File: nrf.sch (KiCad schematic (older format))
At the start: 6 parts, among them SW1 SW_DPST_x2, U1 BLYST-NRF52832-NANO, U2 Oled_128x64_SSD1306

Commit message: More power setup
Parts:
- added SW2: MID, my-fp-library:Tact_SW_3x6x3.5, symbol Switch:SW_DPST_x2
- added SW3: DWN, my-fp-library:Tact_SW_3x6x3.5, symbol Switch:SW_DPST_x2
- SW1: value SW_DPST_x2 -> UP; footprint Buttons_Switches_SMD:SW_DIP_x2_W5.08mm_Slide_Copal_CHS-A -> my-fp-library:Tact_SW_3x6x3.5
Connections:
- net labels added: BTN_2, BTN_3, I2C_SCL, I2C_SDA, SCL, SDA
- wire segments 55 -> 66
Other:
- moved on the sheet: SW1A
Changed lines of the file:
@@
 L Switch:SW_DPST_x2 SW1
 U 1 1 5D072A19
-P 1200 2450
-F 0 "SW1" H 1200 2685 50  0000 C CNN
-F 1 "SW_DPST_x2" H 1200 2594 50  0000 C CNN
-F 2 "Buttons_Switches_SMD:SW_DIP_x2_W5.08mm_Slide_Copal_CHS-A" H 1200 2450 50  0001 C CNN
-F 3 "" H 1200 2450 50  0001 C CNN
-	1    1200 2450
+P 5150 1150
+F 0 "SW1" H 5150 1385 50  0000 C CNN
+F 1 "UP" H 5150 1294 50  0000 C CNN
+F 2 "my-fp-library:Tact_SW_3x6x3.5" H 5150 1150 50  0001 C CNN
+F 3 "" H 5150 1150 50  0001 C CNN
+	1    5150 1150
 	1    0    0    -1
 $EndComp
@@
 L power:GND #PWR0101
 U 1 1 5D072B76
-P 850 2650
-F 0 "#PWR0101" H 850 2400 50  0001 C CNN
-F 1 "GND" H 855 2477 50  0000 C CNN
-F 2 "" H 850 2650 50  0001 C CNN
-F 3 "" H 850 2650 50  0001 C CNN
-	1    850  2650
+P 4550 2200
+F 0 "#PWR0101" H 4550 1950 50  0001 C CNN
+F 1 "GND" H 4555 2027 50  0000 C CNN
+F 2 "" H 4550 2200 50  0001 C CNN
+F 3 "" H 4550 2200 50  0001 C CNN
+	1    4550 2200
 	1    0    0    -1
 $EndComp
-Wire Wire Line
-	1000 2450 850  2450
-Wire Wire Line
-	850  2450 850  2650
 Text GLabel 3550 1350 2    50   Output ~ 0
 MOTOR_PWM
@@
 F1 "accelerometer.sch" 50
 $EndSheet
+$Comp
+L Switch:SW_DPST_x2 SW3
+U 1 1 5D0B8B59
+P 5150 1950
+F 0 "SW3" H 5150 2185 50  0000 C CNN
+F 1 "DWN" H 5150 2094 50  0000 C CNN
+F 2 "my-fp-library:Tact_SW_3x6x3.5" H 5150 1950 50  0001 C CNN
+F 3 "" H 5150 1950 50  0001 C CNN
+	1    5150 1950
+	1    0    0    -1
+$EndComp
+Wire Wire Line
+	5350 1950 5850 1950
+Wire Wire Line
+	5350 1550 5850 1550
+Wire Wire Line
+	5350 1150 5850 1150
+Wire Wire Line
+	4950 1950 4550 1950
+Wire Wire Line
+	4550 1950 4550 2200
+Wire Wire Line
+	4950 1550 4550 1550
+Wire Wire Line
+	4550 1550 4550 1950
+Connection ~ 4550 1950
+Wire Wire Line
+	4950 1150 4550 1150
+Wire Wire Line
+	4550 1150 4550 1550
+Connection ~ 4550 1550
+Text Label 5600 1150 0    50   ~ 0
+BTN_1
+Text Label 5600 1550 0    50   ~ 0
+BTN_2
+Text Label 5600 1950 0    50   ~ 0
+BTN_3
+Wire Wire Line
+	1800 2550 1400 2550
+Wire Wire Line
+	1800 2350 1400 2350
+Text Label 1450 2550 0    50   ~ 0
+BTN_2
+Text Label 1450 2350 0    50   ~ 0
+BTN_3
+Wire Wire Line
+	1800 1350 1400 1350
+Wire Wire Line
+	1800 1450 1400 1450
+Text Label 1450 1350 0    50   ~ 0
+SDA
+Text Label 1450 1450 0    50   ~ 0
+SCL
+Text GLabel 1400 1450 0    50   Output ~ 0
+I2C_SCL
+Text GLabel 1400 1350 0    50   Output ~ 0
+I2C_SDA
+$Comp
+L Switch:SW_DPST_x2 SW2
+U 1 1 5D0D8973
+P 5150 1550
+F 0 "SW2" H 5150 1785 50  0000 C CNN
+F 1 "MID" H 5150 1694 50  0000 C CNN
+F 2 "my-fp-library:Tact_SW_3x6x3.5" H 5150 1550 50  0001 C CNN
+F 3 "" H 5150 1550 50  0001 C CNN
+	1    5150 1550
+	1    0    0    -1
+$EndComp
 $EndSCHEMATC

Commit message: Connectors
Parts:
- added J2: Conn_01x05, Pin_Headers:Pin_Header_Straight_1x05_Pitch1.27mm, symbol Connector_Generic:Conn_01x05
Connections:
- net labels added: RESET, SWDCLK, SWDIO
- net labels removed: GND, VDD
- wire segments 66 -> 79
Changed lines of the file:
@@
-	1    0    0    -1
-$EndComp
-$Comp
-L power:GND #PWR0102
-U 1 1 5CE49E1D
-P 7500 2050
-F 0 "#PWR0102" H 7500 1800 50  0001 C CNN
-F 1 "GND" H 7505 1877 50  0000 C CNN
-F 2 "" H 7500 2050 50  0001 C CNN
-F 3 "" H 7500 2050 50  0001 C CNN
-	1    7500 2050
 	1    0    0    -1
 $EndComp
@@
 Wire Wire Line
 	7300 2550 7300 2500
-$Comp
-L power:GND #PWR0103
-U 1 1 5CE4A4F8
-P 7450 2650
-F 0 "#PWR0103" H 7450 2400 50  0001 C CNN
-F 1 "GND" H 7455 2477 50  0000 C CNN
-F 2 "" H 7450 2650 50  0001 C CNN
-F 3 "" H 7450 2650 50  0001 C CNN
-	1    7450 2650
-	1    0    0    -1
-$EndComp
 Wire Wire Line
 	8100 2750 7750 2750
@@
 Wire Wire Line
 	7750 2650 7450 2650
-$Comp
-L power:VDD #PWR0105
-U 1 1 5CE4AA70
-P 7300 2500
-F 0 "#PWR0105" H 7300 2350 50  0001 C CNN
-F 1 "VDD" H 7317 2673 50  0000 C CNN
-F 2 "" H 7300 2500 50  0001 C CNN
-F 3 "" H 7300 2500 50  0001 C CNN
-	1    7300 2500
-	1    0    0    -1
-$EndComp
-$Comp
-L power:GND #PWR0106
-U 1 1 5CE4AB71
-P 7400 3150
-F 0 "#PWR0106" H 7400 2900 50  0001 C CNN
-F 1 "GND" H 7405 2977 50  0000 C CNN
-F 2 "" H 7400 3150 50  0001 C CNN
-F 3 "" H 7400 3150 50  0001 C CNN
-	1    7400 3150
-	1    0    0    -1
-$EndComp
 Wire Wire Line
 	8100 3150 8050 3150
@@
 Text Label 7750 3850 0    50   ~ 0
 MOSI
-$Comp
-L power:GND #PWR01
-U 1 1 5CE4E69E
-P 7450 4200
-F 0 "#PWR01" H 7450 3950 50  0001 C CNN
-F 1 "GND" H 7455 4027 50  0000 C CNN
-F 2 "" H 7450 4200 50  0001 C CNN
-F 3 "" H 7450 4200 50  0001 C CNN
-	1    7450 4200
-	1    0    0    -1
-$EndComp
 Wire Wire Line
 	8000 4050 7450 4050
@@
 Wire Wire Line
 	7450 4550 7450 4600
-$Comp
-L power:GND #PWR02
-U 1 1 5CE53560
-P 7450 5000
-F 0 "#PWR02" H 7450 4750 50  0001 C CNN
-F 1 "GND" H 7455 4827 50  0000 C CNN
-F 2 "" H 7450 5000 50  0001 C CNN
-F 3 "" H 7450 5000 50  0001 C CNN
-	1    7450 5000
-	1    0    0    -1
-$EndComp
 Wire Wire Line
 	7450 4900 7450 5000
-$Comp
-L power:GND #PWR03
-U 1 1 5CE53F0B
-P 7900 5050
-F 0 "#PWR03" H 7900 4800 50  0001 C CNN
-F 1 "GND" H 7905 4877 50  0000 C CNN
-F 2 "" H 7900 5050 50  0001 C CNN
-F 3 "" H 7900 5050 50  0001 C CNN
-	1    7900 5050
-	1    0    0    -1
-$EndComp
 Wire Wire Line
 	8100 4850 7900 4850
@@
 Wire Wire Line
 	7900 4950 7900 5050
-$Comp
-L power:VDD #PWR0104
-U 1 1 5CE5A0A2
-P 7200 2850
-F 0 "#PWR0104" H 7200 2700 50  0001 C CNN
-F 1 "VDD" H 7217 3023 50  0000 C CNN
-F 2 "" H 7200 2850 50  0001 C CNN
-F 3 "" H 7200 2850 50  0001 C CNN
-	1    7200 2850
-	1    0    0    -1
-$EndComp
 Wire Wire Line
 	8100 2850 7200 2850
@@
 	1    0    0    -1
 $EndComp
-$Comp
-L power:GND #PWR0101
-U 1 1 5D072B76
-P 4550 2200
-F 0 "#PWR0101" H 4550 1950 50  0001 C CNN
-F 1 "GND" H 4555 2027 50  0000 C CNN
-F 2 "" H 4550 2200 50  0001 C CNN
-F 3 "" H 4550 2200 50  0001 C CNN
-	1    4550 2200
-	1    0    0    -1
-$EndComp
 Text GLabel 3550 1350 2    50   Output ~ 0
 MOTOR_PWM
@@
 	4950 1950 4550 1950
 Wire Wire Line
-	4550 1950 4550 2200
-Wire Wire Line
 	4950 1550 4550 1550
 Wire Wire Line
 	4550 1550 4550 1950
-Connection ~ 4550 1950
 Wire Wire Line
 	4950 1150 4550 1150
@@
 Text Label 1450 1350 0    50   ~ 0
 SDA
-Text Label 1450 1450 0    50   ~ 0
-SCL
-Text GLabel 1400 1450 0    50   Output ~ 0
+Text GLabel 1400 1550 0    50   Output ~ 0
 I2C_SCL
 Text GLabel 1400 1350 0    50   Output ~ 0
@@
 	1    0    0    -1
 $EndComp
+$Comp
+L Connector_Generic:Conn_01x05 J2
+U 1 1 5D0EA690
+P 5000 3300
+F 0 "J2" H 5080 3342 50  0000 L CNN
+F 1 "Conn_01x05" H 5080 3251 50  0000 L CNN
+F 2 "Pin_Headers:Pin_Header_Straight_1x05_Pitch1.27mm" H 5000 3300 50  0001 C CNN
+F 3 "~" H 5000 3300 50  0001 C CNN
+	1    5000 3300
+	1    0    0    -1
+$EndComp
+Connection ~ 4550 1950
+Wire Wire Line
+	4550 1950 4550 2200
+$Comp
+L power:(GND) #PWR01
+U 1 1 5D0FADC1
+P 4550 2200
+F 0 "#PWR01" H 4550 2200 30  0001 C CNN
+F 1 "(GND)" H 4550 2200 30  0001 C CNN
+F 2 "" H 4550 2200 60  0000 C CNN
+F 3 "" H 4550 2200 60  0000 C CNN
+	1    4550 2200
+	1    0    0    -1
+$EndComp
+$Comp
+L power:(GND) #PWR011
+U 1 1 5D0FAF36
+P 7450 2700
+F 0 "#PWR011" H 7450 2700 30  0001 C CNN
+F 1 "(GND)" H 7450 2700 30  0001 C CNN
+F 2 "" H 7450 2700 60  0000 C CNN
+F 3 "" H 7450 2700 60  0000 C CNN
+	1    7450 2700
+	1    0    0    -1
+$EndComp
+$Comp
+L power:(GND) #PWR010
+U 1 1 5D0FAF53
+P 7400 3200
+F 0 "#PWR010" H 7400 3200 30  0001 C CNN
+F 1 "(GND)" H 7400 3200 30  0001 C CNN
+F 2 "" H 7400 3200 60  0000 C CNN
+F 3 "" H 7400 3200 60  0000 C CNN
+	1    7400 3200
+	1    0    0    -1
+$EndComp
+$Comp
+L power:(GND) #PWR014
+U 1 1 5D0FAF7A
+P 7500 2100
+F 0 "#PWR014" H 7500 2100 30  0001 C CNN
+F 1 "(GND)" H 7500 2100 30  0001 C CNN
+F 2 "" H 7500 2100 60  0000 C CNN
+F 3 "" H 7500 2100 60  0000 C CNN
+	1    7500 2100
+	1    0    0    -1
+$EndComp
+Wire Wire Line
+	7500 2050 7500 2100
+Wire Wire Line
+	7450 2650 7450 2700
+Wire Wire Line
+	7400 3150 7400 3200
+$Comp
+L power:(GND) #PWR012
+U 1 1 5D0FFE5A
+P 7450 4200
+F 0 "#PWR012" H 7450 4200 30  0001 C CNN
+F 1 "(GND)" H 7450 4200 30  0001 C CNN
+F 2 "" H 7450 4200 60  0000 C CNN
+F 3 "" H 7450 4200 60  0000 C CNN
+	1    7450 4200
+	1    0    0    -1
+$EndComp
+$Comp
+L power:(GND) #PWR013
+U 1 1 5D0FFE77
+P 7450 5000
+F 0 "#PWR013" H 7450 5000 30  0001 C CNN
+F 1 "(GND)" H 7450 5000 30  0001 C CNN
+F 2 "" H 7450 5000 60  0000 C CNN
+F 3 "" H 7450 5000 60  0000 C CNN
+	1    7450 5000
+	1    0    0    -1
+$EndComp
+$Comp
+L power:(GND) #PWR015
+U 1 1 5D0FFEAF
+P 7900 5050
+F 0 "#PWR015" H 7900 5050 30  0001 C CNN
+F 1 "(GND)" H 7900 5050 30  0001 C CNN
+F 2 "" H 7900 5050 60  0000 C CNN
+F 3 "" H 7900 5050 60  0000 C CNN
+	1    7900 5050
+	1    0    0    -1
+$EndComp
+$Comp
+L power:+3.3 #PWR09
+U 1 1 5D100235
+P 7300 2500
+F 0 "#PWR09" H 7300 2550 30  0001 C CNN
+F 1 "+3.3" H 7300 2633 50  0000 C CNN
+F 2 "" H 7300 2500 60  0000 C CNN
+F 3 "" H 7300 2500 60  0000 C CNN
+	1    7300 2500
+	1    0    0    -1
+$EndComp
+$Comp
+L power:+3.3 #PWR08
+U 1 1 5D1002BF
+P 7200 2850
+F 0 "#PWR08" H 7200 2900 30  0001 C CNN
+F 1 "+3.3" H 7200 2983 50  0000 C CNN
+F 2 "" H 7200 2850 60  0000 C CNN
+F 3 "" H 7200 2850 60  0000 C CNN
+	1    7200 2850
+	1    0    0    -1
+$EndComp
+$Comp
+L power:(GND) #PWR03
+U 1 1 5D1005C9
+P 4700 3750
+F 0 "#PWR03" H 4700 3750 30  0001 C CNN
+F 1 "(GND)" H 4700 3750 30  0001 C CNN
+F 2 "" H 4700 3750 60  0000 C CNN
+F 3 "" H 4700 3750 60  0000 C CNN
+	1    4700 3750
+	1    0    0    -1
+$EndComp
+$Comp
+L power:+3.3 #PWR02
+U 1 1 5D1005E6
+P 4700 2950
+F 0 "#PWR02" H 4700 3000 30  0001 C CNN
+F 1 "+3.3" H 4700 3083 50  0000 C CNN
+F 2 "" H 4700 2950 60  0000 C CNN
+F 3 "" H 4700 2950 60  0000 C CNN
+	1    4700 2950
+	1    0    0    -1
+$EndComp
+Wire Wire Line
+	4800 3100 4700 3100
+Wire Wire Line
+	4700 3100 4700 2950
+Wire Wire Line
+	4800 3500 4700 3500
+Wire Wire Line
+	4700 3500 4700 3750
+Wire Wire Line
+	4800 3400 4400 3400
+Wire Wire Line
+	1800 1550 1400 1550
+Text Label 1450 1550 0    50   ~ 0
+SCL
+Text Label 1450 1450 0    50   ~ 0
+RESET
+Text Label 4450 3400 0    50   ~ 0
+RESET
+Wire Wire Line
+	4800 3300 4400 3300
+Wire Wire Line
+	4800 3200 4400 3200
+Wire Wire Line
+	2550 3350 2550 3750
+Wire Wire Line
+	2650 3350 2650 3750
+Text Label 2550 3700 1    50   ~ 0
+SWDIO
+Text Label 2650 3700 1    50   ~ 0
+SWDCLK
+Text Label 4450 3300 0    50   ~ 0
+SWDCLK
+Text Label 4450 3200 0    50   ~ 0
+SWDIO
 $EndSCHEMATC

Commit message: New PCB's
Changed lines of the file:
@@
 	8100 2850 7200 2850
 $Sheet
-S 650  7000 1050 600
+S 650  6950 1050 600
 U 5D059B17
 F0 "vibration_motor" 50

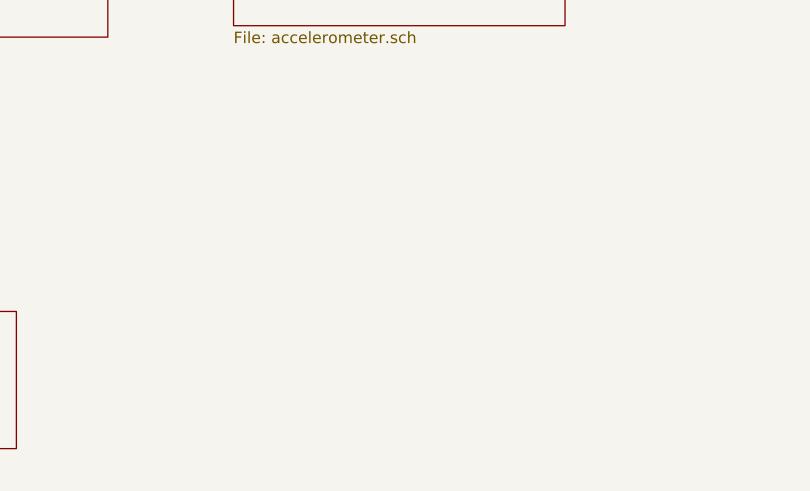
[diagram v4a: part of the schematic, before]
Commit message: Implement 240x240 IPS display
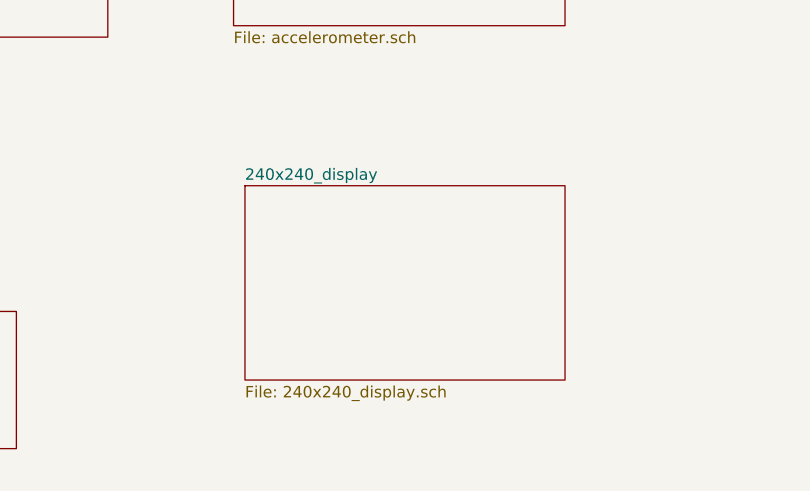
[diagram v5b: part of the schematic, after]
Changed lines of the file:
@@
 $Descr A4 11693 8268
 encoding utf-8
-Sheet 1 4
+Sheet 1 5
 Title ""
 Date ""
@@
 Text Label 4450 3200 0    50   ~ 0
 SWDIO
+$Sheet
+S 2700 6400 1400 850
+U 5DA394ED
+F0 "240x240_display" 50
+F1 "240x240_display.sch" 50
+$EndSheet
 $EndSCHEMATC

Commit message: Initial
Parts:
- removed C1, C2: C, Capacitors_SMD:C_0805, symbol Device:C
- removed U1: BLYST-NRF52832-NANO, my-fp-library:BLYST NRF52832-NANO, symbol nordic:BLYST-NRF52832-NANO
- removed U2: Oled_128x64_SSD1306, my-fp-library:oled ssd1306 29x0.7mm, symbol oleds:Oled_128x64_SSD1306
- added C1, C10: 22pF, Capacitors_SMD:C_0603_HandSoldering, symbol Device:C_Small
- added C11, C2: 1uF, Capacitors_SMD:C_0603_HandSoldering, symbol Device:C_Small
- added C12: 10uF, Capacitors_SMD:C_0603_HandSoldering, symbol Device:C_Small
- added C8: 0.1uF, Capacitors_SMD:C_0603_HandSoldering, symbol Device:C_Small
- added D4: ZLLS410, Diodes_SMD:D_SOD-323, symbol _semi:DIODE
- added IC2: 113990582, SamacSys_Parts:113990582, symbol SamacSys_Parts:113990582
- added J7: Conn_01x12, symbol Connector_Generic:Conn_01x12
- added Q1, Q3, Q4: SI3139K, TO_SOT_Packages_SMD:SOT-23, symbol Transistor_FET:TP0610T
- added Q2: MGSF1N02L, TO_SOT_Packages_SMD:SOT-23, symbol Transistor_FET:2N7002
- added R10: 30, Resistors_SMD:R_0603_HandSoldering, symbol Device:R
- added R13: 100, Resistors_SMD:R_0603_HandSoldering, symbol Device:R
- added R17: 10K, Resistors_SMD:R_0603_HandSoldering, symbol Device:R
- added R18, R19: 10K, Resistors_SMD:R_0603_HandSoldering, symbol Device:R_Small
- added R2, R8, R9: 100K, Resistors_SMD:R_0603_HandSoldering, symbol Device:R
- added R3: 2.2K, Resistors_SMD:R_0603_HandSoldering, symbol Device:R
- added unit 2 of SW3
- added SW4: DWN, my-fp-library:Tact_SW_3x6x3.5, symbol Switch:SW_DPST_x2
- added U1: GD25Q16, Package_SO:SOIC-8_3.9x4.9mm_P1.27mm, symbol Memory_Flash:AT25SF081-SSHD-X
- added U2: C0720B001F, my-fp-library:VIBRATION MOTOR COIN 3V FLEX - C0720B001F, symbol vib_motor:C0720B001F
- added X1: 32.768, symbol _passive:CRYSTAL
- R1: value R -> 330; footprint Resistors_SMD:R_0805 -> Resistors_SMD:R_0603_HandSoldering
- SW3: value DWN -> BACK
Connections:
- net labels added: BTN_4, LEDK, LIGHT1, LIGHT2, LIGHT3, QSPI_CS, QSPI_DATA0, QSPI_DATA1, QSPI_DATA2, QSPI_DATA3, QSPI_SCK, SPI_CS, SPI_DC, SPI_RESET, SPI_SCL, SPI_SDA, XL1, XL2
- net labels removed: CS, DC, I2C_SCL, I2C_SDA, MOSI, RES, SCK
- wire segments 79 -> 152
